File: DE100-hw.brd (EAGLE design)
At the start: 160 x 100 mm, 50 parts, among them IC3 74HC14D, IC4 74HC14D, U1 TLP521-4(GB), U2 TLP521-4(GB), X1 22-23-2041, X2 22-23-2031, X3 22-23-2101

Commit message: change route
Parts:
- removed H3: MOUNT-PAD-SQUARE3.0, holes:3,0-PAD-SQUARE
- moved R25 6.90 mm to (49.9, 35.3), turned to 0 degrees
- moved R24 3.64 mm to (49.9, 32.9), turned to 0 degrees
- moved R1 3.42 mm to (45.2, 45.0)
- moved R2 3.42 mm to (45.2, 42.9)
- moved R3 3.42 mm to (45.2, 40.7)
- moved R4 3.42 mm to (45.3, 38.6)
- moved R9 3.38 mm to (45.3, 32.1)
- moved R10 3.38 mm to (45.3, 30.0)
- moved R11 3.38 mm to (45.3, 27.8)
- moved X3 2.48 mm to (38.0, 34.1)
- moved X2 2.06 mm to (106.5, 16.4)
- moved X1 2.00 mm to (94.8, 16.4)
- moved J1 1.50 mm to (44.6, 50.5)
- moved R23 1.33 mm to (49.9, 30.5), turned to 0 degrees
- moved IC4 1.00 mm to (77.5, 23.4)
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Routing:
- net VCC-ISO: track 95.7 -> 85.5 mm
- net +5V: track 319.6 -> 326.9 mm
- net N$52: track 21.5 -> 17.2 mm
- net N$24: track 8.58 -> 12.3 mm
- net N$25: track 6.20 -> 9.88 mm
- net N$26: track 5.45 -> 9.02 mm
- net N$27: track 6.80 -> 9.51 mm
- net LS-7: track 5.50 -> 8.04 mm
- net N$51: track 16.7 -> 14.4 mm
- net GND-ISO: track 15.6 -> 14.1 mm
- net LIN-4: track 65.4 -> 66.6 mm
- net LS-3: track 7.70 -> 6.65 mm
- net TX-RFID: track 28.0 -> 29.0 mm
- net N$35: track 7.19 -> 8.19 mm
- net N$23: track 4.74 -> 5.74 mm
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
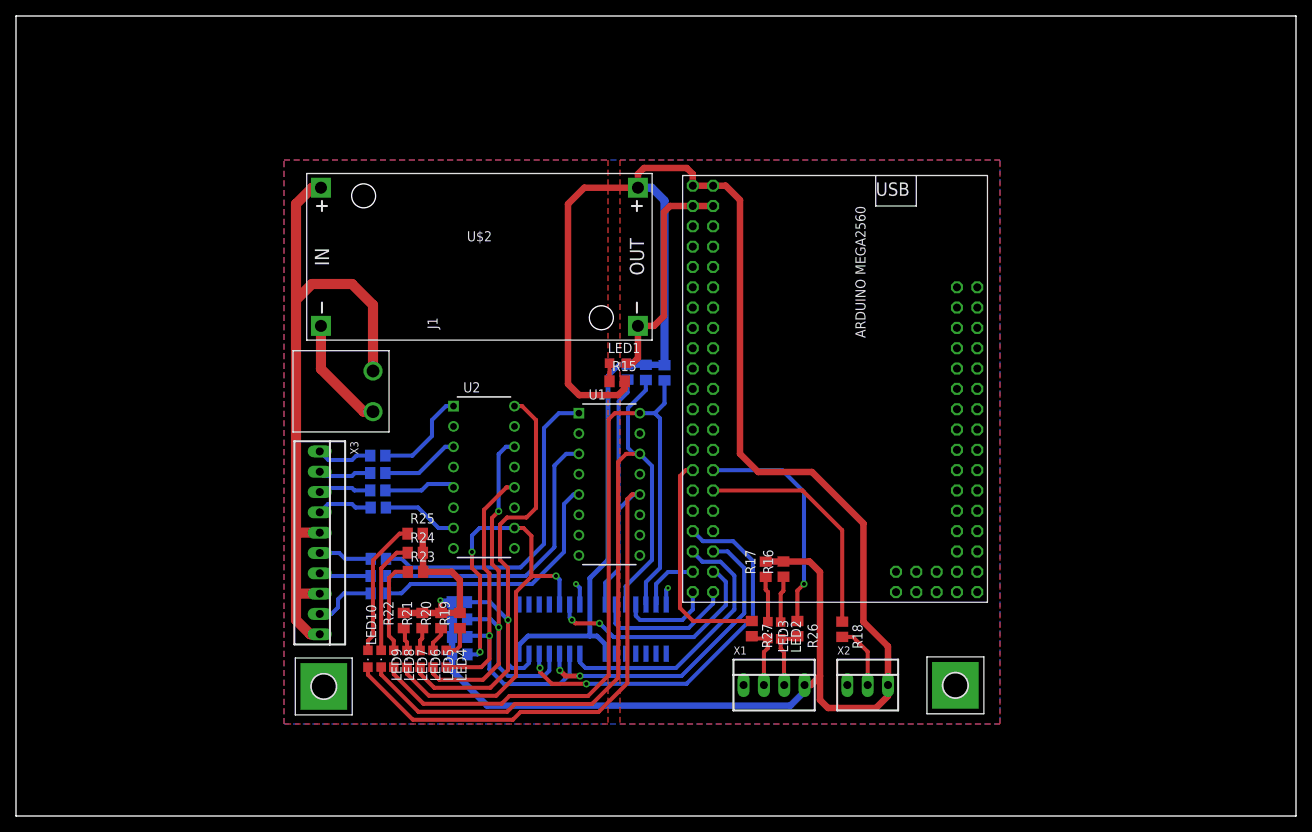
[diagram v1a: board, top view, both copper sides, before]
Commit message: add additional name and gerber file
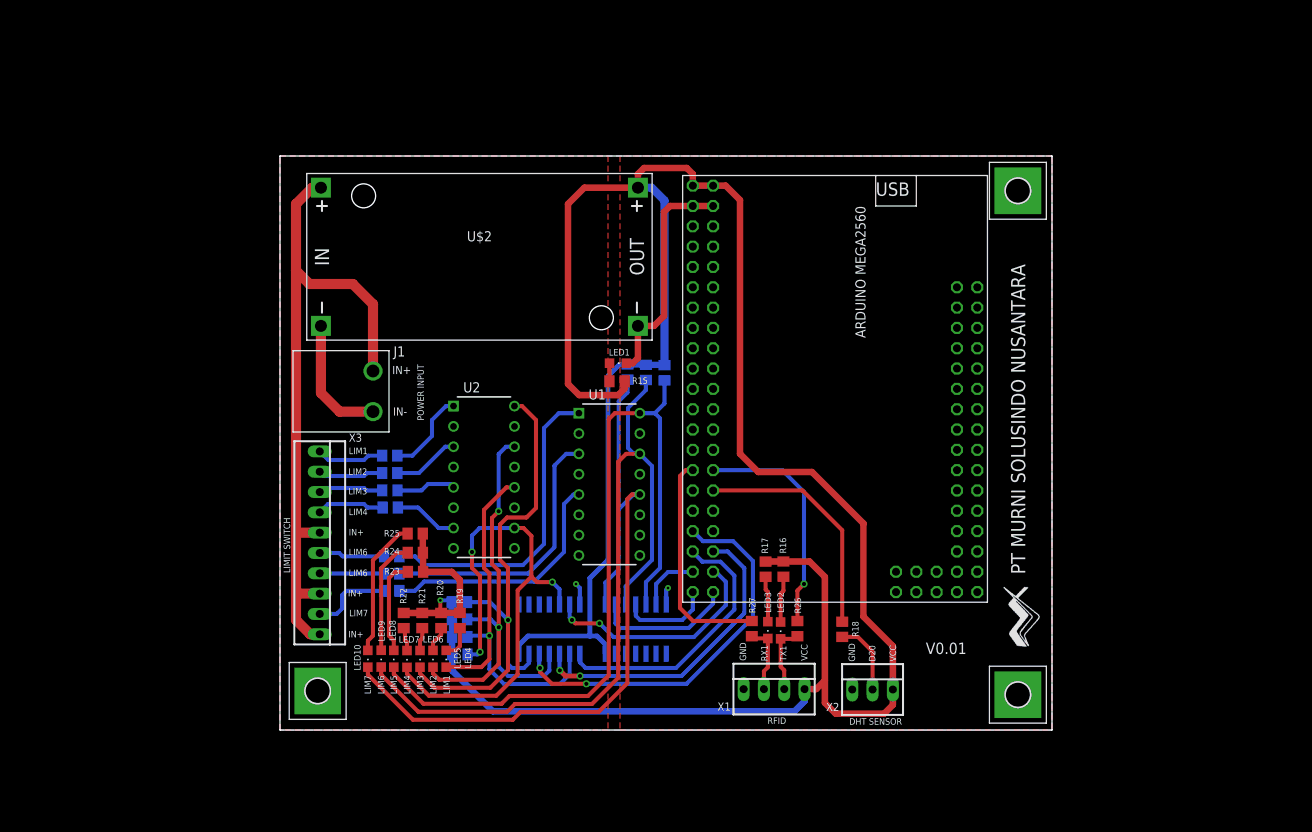
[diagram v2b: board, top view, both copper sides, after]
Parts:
- added H3: MOUNT-PAD-SQUARE3.0, holes:3,0-PAD-SQUARE
- moved H2 7.90 mm to (125.2, 15.2)
- moved R10 1.70 mm to (47.0, 30.3)
- moved R11 1.70 mm to (47.0, 28.1)
- moved R9 1.70 mm to (47.0, 32.5)
- moved R1 1.50 mm to (46.7, 45.0)
- moved R2 1.50 mm to (46.7, 42.9)
- moved R3 1.50 mm to (46.7, 40.7)
- moved R4 1.50 mm to (46.8, 38.6)
- moved H1 0.94 mm to (37.7, 15.6)
- moved X2 0.83 mm to (107.1, 15.8)
- moved X1 0.51 mm to (94.8, 15.9)
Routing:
- net +5V: track 326.9 -> 330.2 mm
- net LS-7: track 8.04 -> 10.2 mm
- net N$34: track 32.8 -> 30.9 mm
- net N$33: track 36.4 -> 34.6 mm
- net N$32: track 41.0 -> 39.2 mm
- net GND-ISO: track 14.1 -> 15.9 mm
- net LS-6: track 6.51 -> 8.06 mm
- net LS-5: track 6.68 -> 8.23 mm
- net N$24: track 12.3 -> 10.8 mm
- net LS-3: track 6.65 -> 8.15 mm
- net LS-1: track 6.97 -> 8.47 mm
- net N$27: track 9.51 -> 8.01 mm
- net N$25: track 9.88 -> 8.38 mm
- net LS-2: track 6.68 -> 8.18 mm
- net LS-4: track 6.98 -> 8.48 mm
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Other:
- board size 160 x 100 mm -> 96.5 x 71.8 mm
- board text added: "D20"
- board text added: "DHT SENSOR"
- board text added: "GND"
- board text added: "IN+"
- board text added: "IN-"
- board text added: "LIM1"
- board text added: "LIM2"
- board text added: "LIM3"
- board text added: "LIM4"
- board text added: "LIM5"
- board text added: "LIM6"
- board text added: "LIM7"
- board text added: "LIMIT SWITCH"
- board text added: "POWER INPUT"
- board text added: "PT MURNI SOLUSINDO NUSANTARA"
- board text added: "RFID"
- board text added: "RX1"
- board text added: "TX1"
- board text added: "V0.01"
- board text added: "VCC"

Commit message: add hole
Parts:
- added H4: MOUNT-PAD-SQUARE3.0, holes:3,0-PAD-SQUARE
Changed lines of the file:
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@@
 <attribute name="MF" value="Toshiba" x="81.3582" y="-37.6629" size="1.778" layer="27" display="off"/>
 <attribute name="MP" value="TLP521-4_GB_" x="81.3582" y="-37.6629" size="1.778" layer="27" display="off"/>
-<attribute name="NAME" x="55.8982" y="52.9471" size="1.27" layer="25"/>
+<attribute name="NAME" x="60.013" y="52.8455" size="1.27" layer="25"/>
 <attribute name="PACKAGE" value="DIP-16 Toshiba" x="81.3582" y="-37.6629" size="1.778" layer="27" display="off"/>
 <attribute name="PRICE" value="None" x="81.3582" y="-37.6629" size="1.778" layer="27" display="off"/>
@@
 <attribute name="POPULARITY" value="0" x="125.2349" y="78.1534" size="1.778" layer="27" display="off"/>
 </element>
+<element name="H4" library="holes" library_urn="urn:adsk.eagle:library:237" package="3,0-PAD-SQUARE" package3d_urn="urn:adsk.eagle:package:14290/1" value="MOUNT-PAD-SQUARE3.0" x="55.7784" y="56.7436" smashed="yes">
+<attribute name="POPULARITY" value="0" x="55.7784" y="56.7436" size="1.778" layer="27" display="off"/>
+</element>
 </elements>
